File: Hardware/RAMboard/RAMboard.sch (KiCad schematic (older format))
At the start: 4 parts, among them J1 RAMC_L, J2 RAMC_R, U1 FM18W08-SG

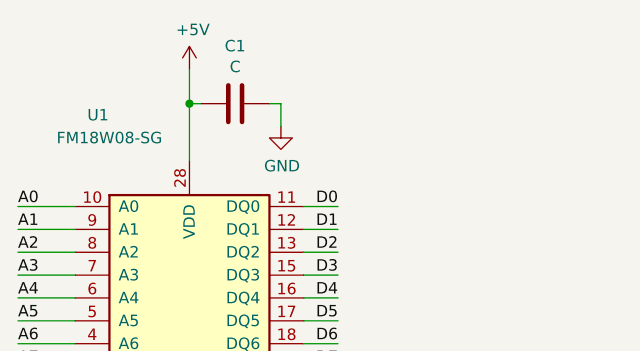
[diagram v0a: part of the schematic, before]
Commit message: Update capacitor value
Specify 100n as the decoupling capacitor value
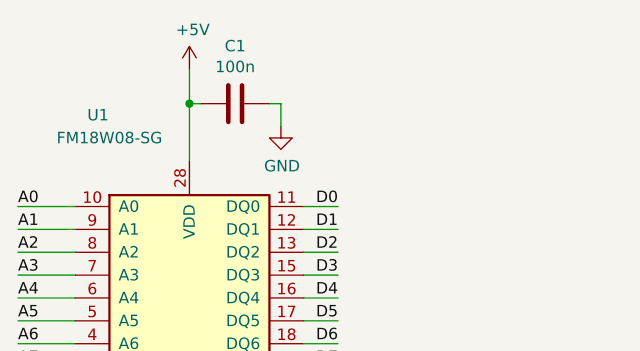
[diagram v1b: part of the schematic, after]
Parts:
- C1: value C -> 100n
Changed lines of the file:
@@
 P 5350 1900
 F 0 "C1" V 5602 1900 50  0000 C CNN
-F 1 "C" V 5511 1900 50  0000 C CNN
+F 1 "100n" V 5511 1900 50  0000 C CNN
 F 2 "Capacitor_THT:CP_Radial_D5.0mm_P2.50mm" H 5388 1750 50  0001 C CNN
 F 3 "~" H 5350 1900 50  0001 C CNN
